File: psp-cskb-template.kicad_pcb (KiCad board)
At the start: 2 copper layers, 90.2 x 95.9 mm, 6 parts, among them J1 Conn_02x26_Odd_Even, J2 Conn_02x26_Odd_Even

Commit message: make pcb 6 layers
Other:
- copper layers 2 -> 6
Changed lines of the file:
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@@
 	(layers
 		(0 "F.Cu" signal)
+		(1 "In1.Cu" signal)
+		(2 "In2.Cu" signal)
+		(3 "In3.Cu" signal)
+		(4 "In4.Cu" signal)
 		(31 "B.Cu" signal)
 		(32 "B.Adhes" user "B.Adhesive")
@@
 	)
 	(setup
+		(stackup
+			(layer "F.SilkS"
+				(type "Top Silk Screen")
+			)
+			(layer "F.Paste"
+				(type "Top Solder Paste")
+			)
+			(layer "F.Mask"
+				(type "Top Solder Mask")
+				(thickness 0.01)
+			)
+			(layer "F.Cu"
+				(type "copper")
+				(thickness 0.035)
+			)
+			(layer "dielectric 1"
+				(type "prepreg")
+				(thickness 0.1)
+				(material "FR4")
+				(epsilon_r 4.5)
+				(loss_tangent 0.02)
+			)
+			(layer "In1.Cu"
+				(type "copper")
+				(thickness 0.035)
+			)
+			(layer "dielectric 2"
+				(type "core")
+				(thickness 0.535)
+				(material "FR4")
+				(epsilon_r 4.5)
+				(loss_tangent 0.02)
+			)
+			(layer "In2.Cu"
+				(type "copper")
+				(thickness 0.035)
+			)
+			(layer "dielectric 3"
+				(type "prepreg")
+				(thickness 0.1)
+				(material "FR4")
+				(epsilon_r 4.5)
+				(loss_tangent 0.02)
+			)
+			(layer "In3.Cu"
+				(type "copper")
+				(thickness 0.035)
+			)
+			(layer "dielectric 4"
+				(type "core")
+				(thickness 0.535)
+				(material "FR4")
+				(epsilon_r 4.5)
+				(loss_tangent 0.02)
+			)
+			(layer "In4.Cu"
+				(type "copper")
+				(thickness 0.035)
+			)
+			(layer "dielectric 5"
+				(type "prepreg")
+				(thickness 0.1)
+				(material "FR4")
+				(epsilon_r 4.5)
+				(loss_tangent 0.02)
+			)
+			(layer "B.Cu"
+				(type "copper")
+				(thickness 0.035)
+			)
+			(layer "B.Mask"
+				(type "Bottom Solder Mask")
+				(thickness 0.01)
+			)
+			(layer "B.Paste"
+				(type "Bottom Solder Paste")
+			)
+			(layer "B.SilkS"
+				(type "Bottom Silk Screen")
+			)
+			(copper_finish "None")
+			(dielectric_constraints no)
+		)
 		(pad_to_mask_clearance 0)
 		(allow_soldermask_bridges_in_footprints no)

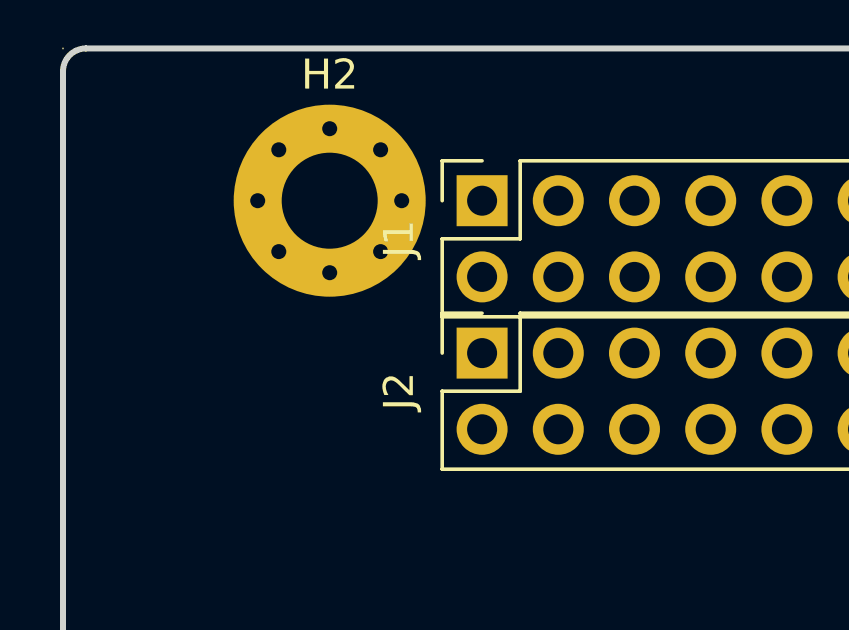
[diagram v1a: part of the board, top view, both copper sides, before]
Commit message: flip CSKB header numbers
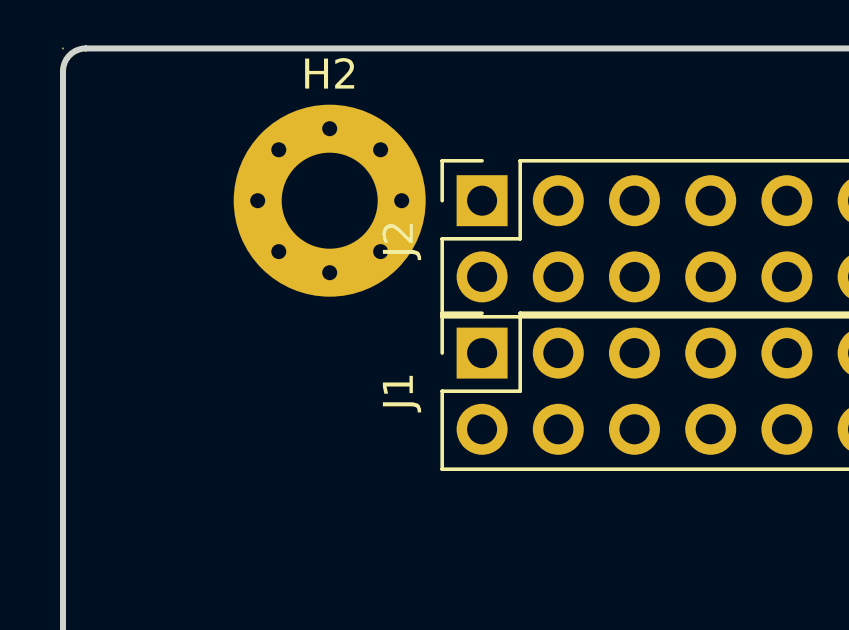
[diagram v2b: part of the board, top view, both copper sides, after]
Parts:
- renumbered J2 to J1, J1 to J2
